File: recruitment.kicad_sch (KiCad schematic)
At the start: 1 part

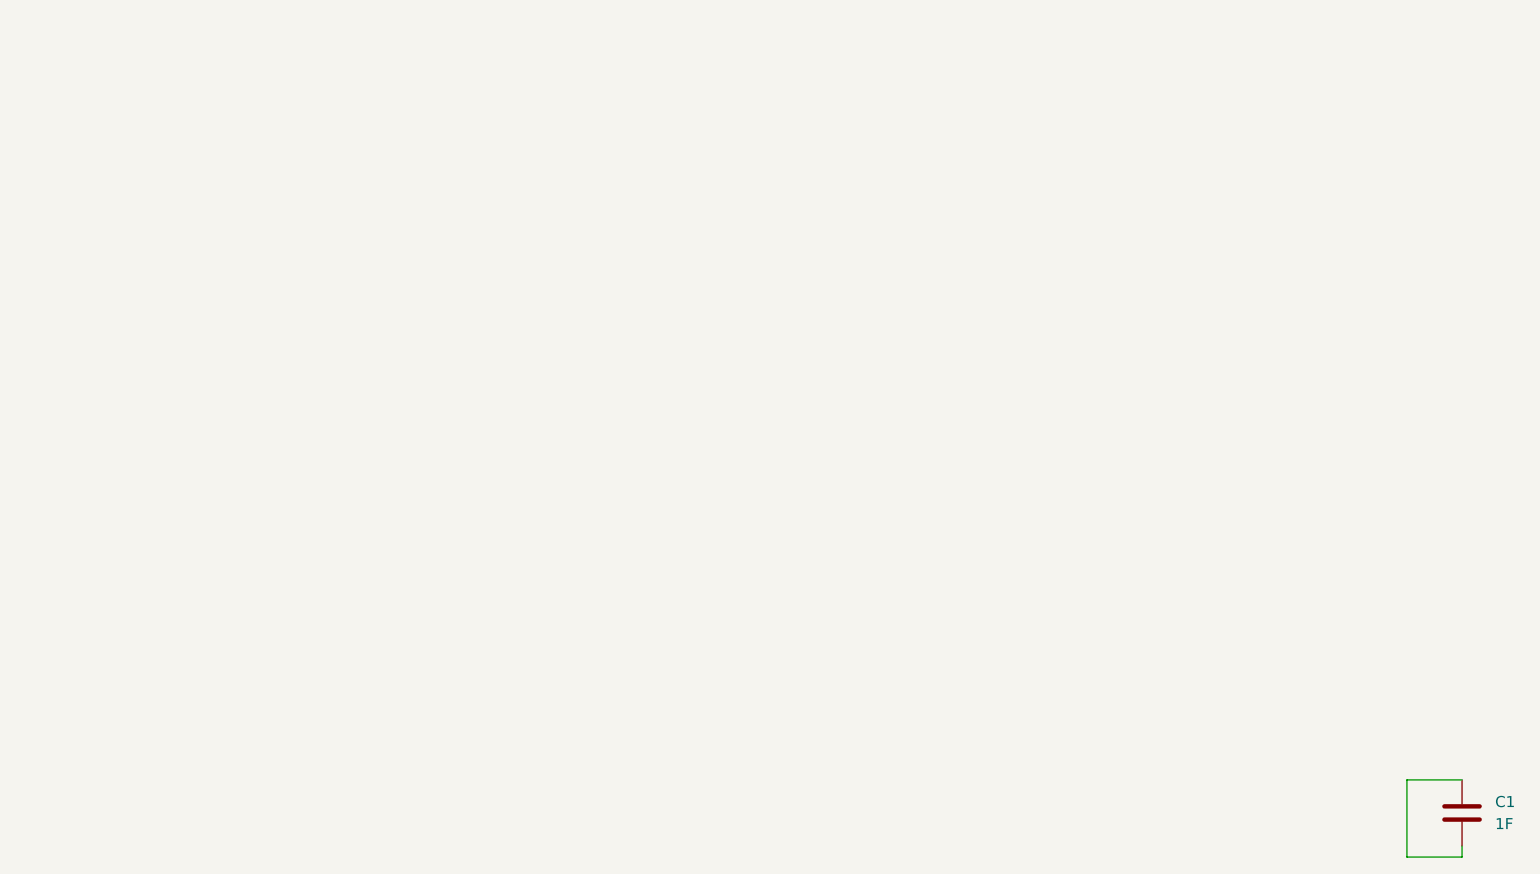
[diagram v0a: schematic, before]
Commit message: added components and hierarchical sheets
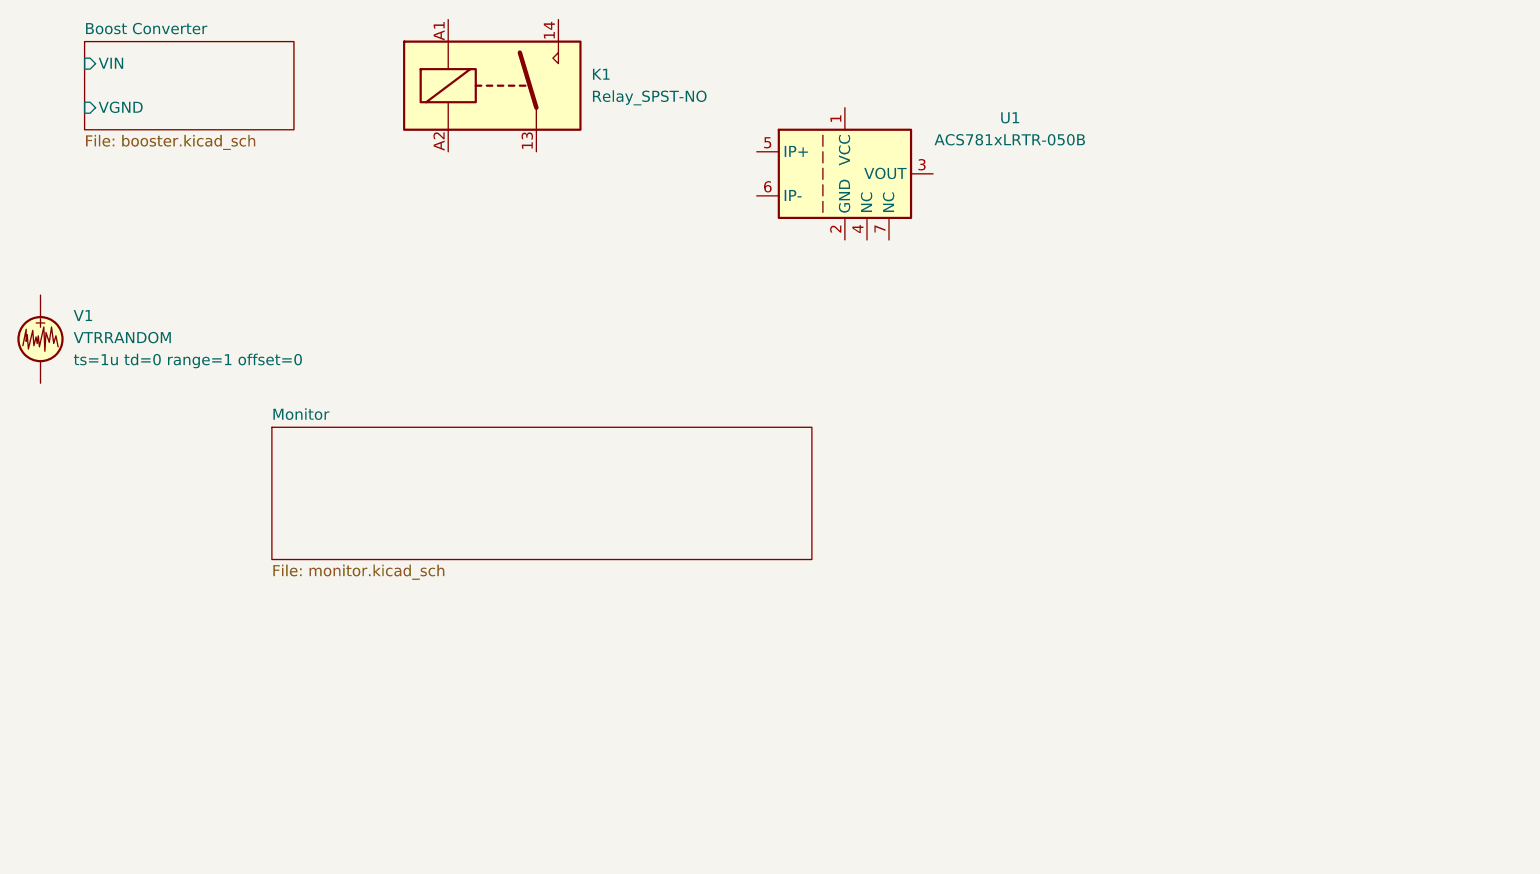
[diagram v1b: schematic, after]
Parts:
- removed C1: 1F, Capacitor_SMD:C_0805_2012Metric, symbol Device:C
- added K1: Relay_SPST-NO, symbol Relay:Relay_SPST-NO
- added U1: ACS781xLRTR-050B, Sensor_Current:Allegro_PSOF-7_4.8x6.4mm_P1.60mm, symbol Sensor_Current:ACS781xLRTR-050B
- added V1: VTRRANDOM, symbol Simulation_SPICE:VTRRANDOM
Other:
- added sheet Boost Converter (booster.kicad_sch)
- added sheet Monitor (monitor.kicad_sch)
